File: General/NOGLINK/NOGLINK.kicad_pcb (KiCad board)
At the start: 2 copper layers, 19.5 x 30.8 mm, 22 parts, among them J1 CAN, J2 SWD/VCP, J3 SPI/I2C/UART, SW1 USR, U1 MIC5365-3.3YC5, U2 STLINK-V3MODS, U3 ATA6561

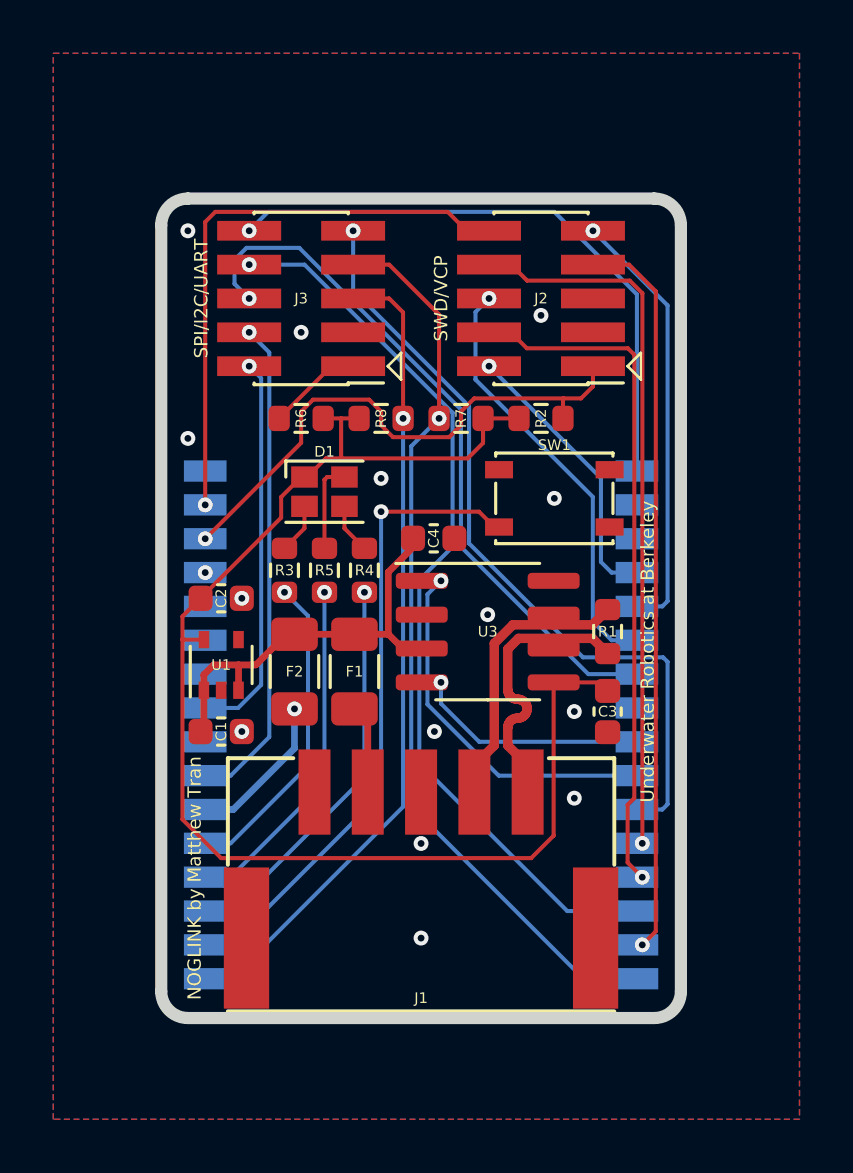
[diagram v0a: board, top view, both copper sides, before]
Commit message: convert to kicad 6
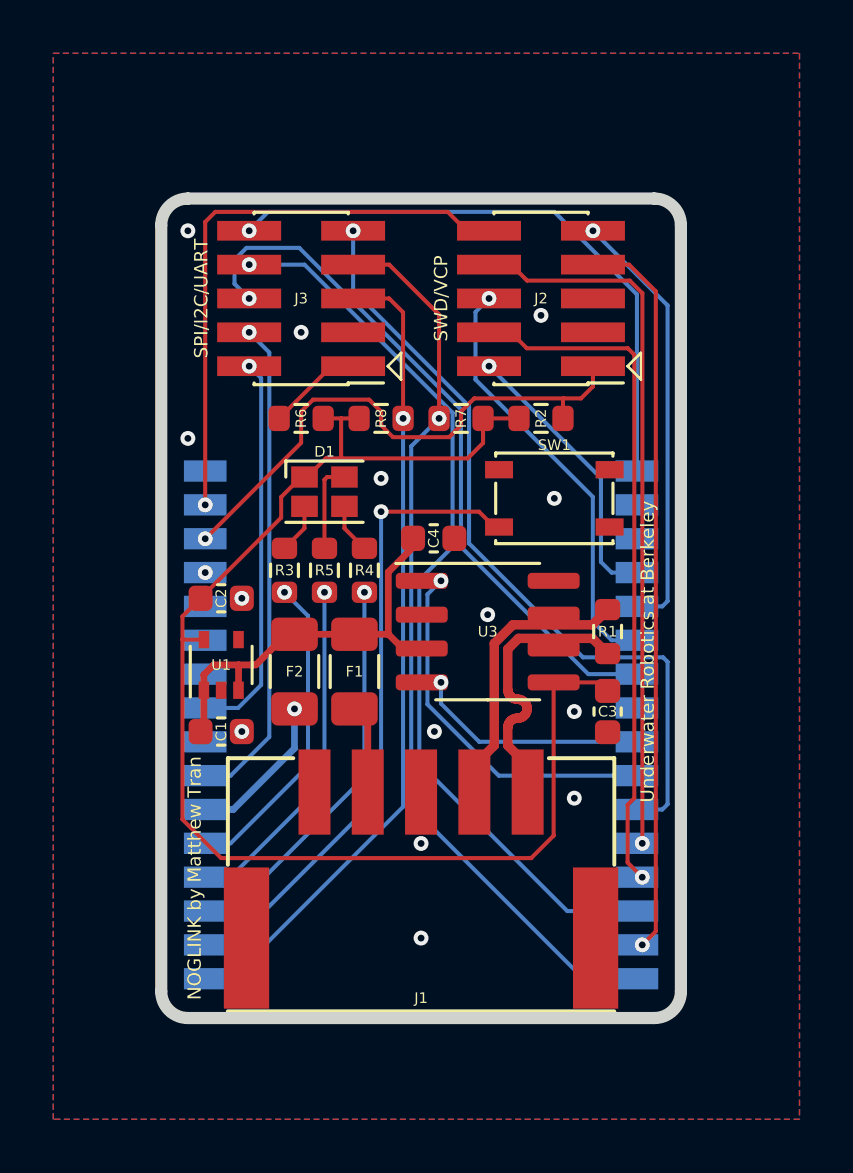
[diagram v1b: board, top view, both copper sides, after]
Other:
- net class Default removed
- net class Power removed
